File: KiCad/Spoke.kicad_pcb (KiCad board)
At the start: 2 copper layers, 50 x 100 mm, 128 parts, among them J1 B2B-PH-K-S, J10 BL-A, J11 BL-C, J12 Amphenol 132289, J2 BAT+, J3 BAT-, J4 GCT USB4105/USB4110, J5 CHG+, J6 CHG-, J7 PLS-1x3, J8 PLS-1x6, J9 PLS-1x3, Q1 AO3407A, Q2 AO3400, Q3 AO3400, Q4 AO3400, SW1 PWR, SW2 OK/UP, SW3 ESC/DN, SW4 BOOT, U1 SP0503BAHTG, U2 TP4056, U3 CP2102N-A02-GQFN28, U4 LM3671MF-3.3, U5 74HC4052PW, U6 STM32F103C8T6, U7 LSM303DLHC, X1 8MHz

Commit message: Add C14
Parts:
- added C14: 47uF, Spoke:C_tantA, B.Cu at (97.8, 89.5)
- moved C20 0.75 mm to (97.0, 91.5)
- renumbered C14 to C15, C15 to C16, C16 to C17, C17 to C18, C18 to C19, C19 to C20, C20 to C21, C21 to C22, C22 to C23, C23 to C24, C24 to C25, C25 to C26, C26 to C27, C27 to C28, C28 to C29, C29 to C30, C30 to C31, C31 to C32, C32 to C33
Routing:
- net +3V3: track 313.7 -> 318.9 mm, vias 14 -> 15
- net LED_RED: track 50.3 -> 52.1 mm
- net USB_RXD: track 85.4 -> 84.8 mm
- net GND: vias 20 -> 21

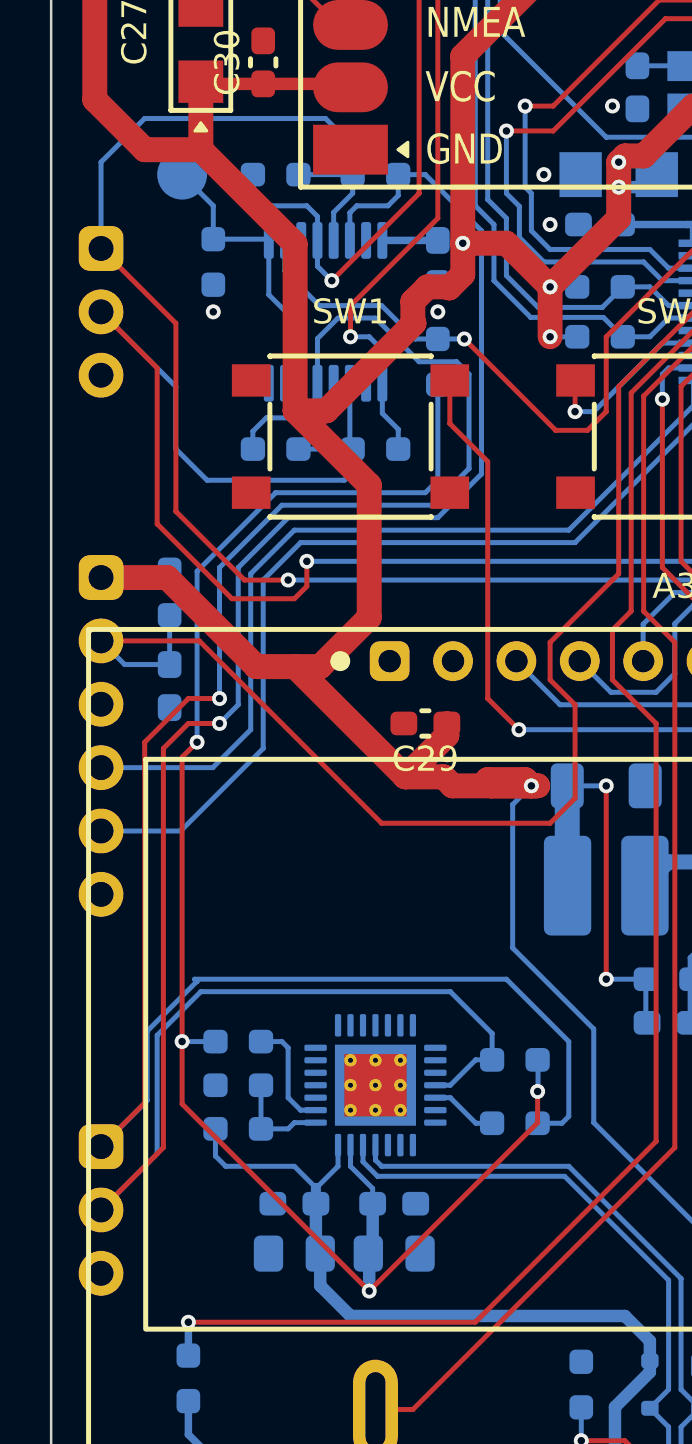
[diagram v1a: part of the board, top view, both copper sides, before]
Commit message: Add TP1, TP2
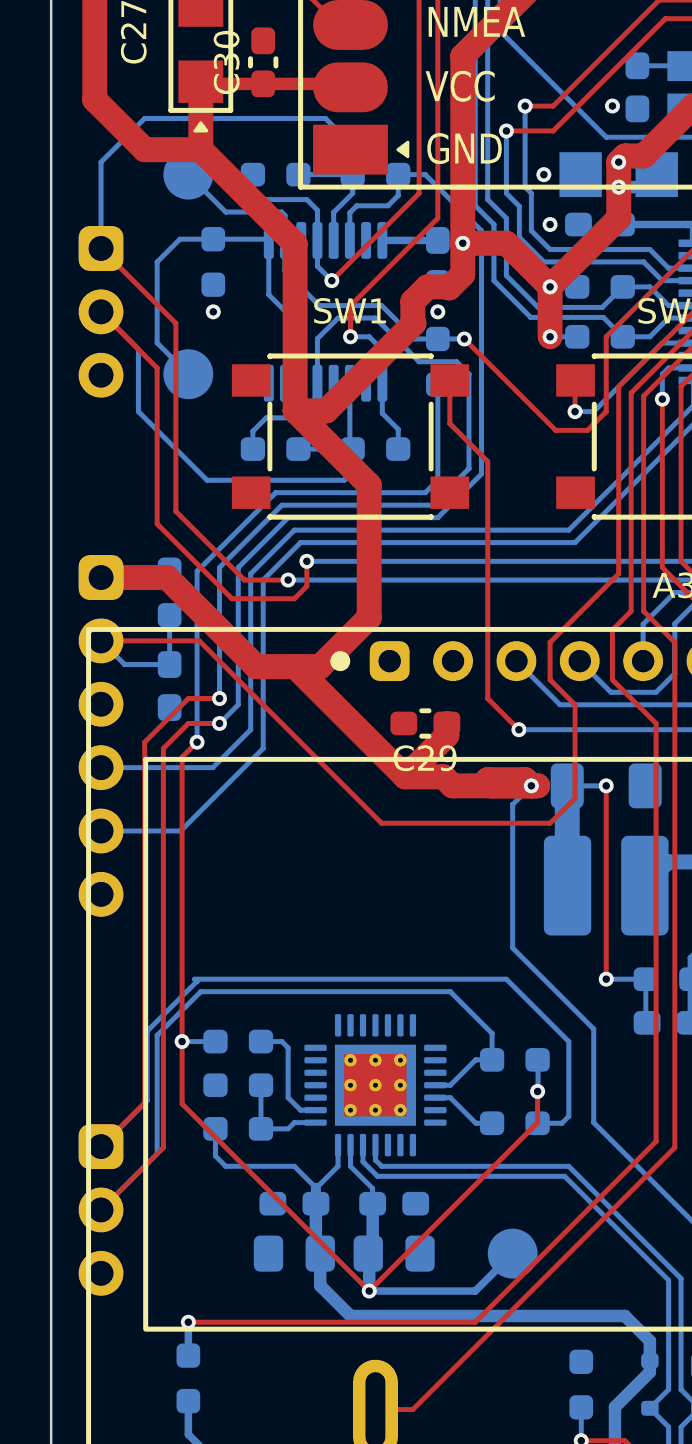
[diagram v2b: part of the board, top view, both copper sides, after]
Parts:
- added TP1: Pad-Round, Spoke:Pad_round, B.Cu at (93.5, 132.8)
- added TP2: Pad-Round, Spoke:Pad_round, B.Cu at (80.5, 89.5)
- moved TP3 8.00 mm to (80.5, 97.5)
- renumbered TP8 to TP10, TP9 to TP11, TP10 to TP12, TP11 to TP13, TP12 to TP14, TP13 to TP15, TP14 to TP16, TP15 to TP17, TP16 to TP18, TP1 to TP3, TP2 to TP4, TP3 to TP5, TP4 to TP6, TP5 to TP7, TP6 to TP8, TP7 to TP9
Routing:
- net VDD: track 66.9 -> 73.3 mm
- net MUX_BLE_USB: track 28.7 -> 34.2 mm
- net Net-(U5-S1): track 11.6 -> 16.2 mm

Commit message: Route BLE
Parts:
- moved TP10 2.75 mm to (79.0, 58.5)
- moved TP11 2.75 mm to (81.8, 58.5)
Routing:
- net +3V3: track 318.9 -> 334.4 mm
- net Net-(A1-SWDCLK): track 0.00 -> 14.4 mm, vias 0 -> 2
- net Net-(A1-SWDIO): track 0.00 -> 13.8 mm, vias 0 -> 2
- net Net-(A1-MODE): track 0.00 -> 8.52 mm
- net Net-(A1-DISC): track 0.00 -> 8.37 mm
- net Net-(A1-WAKEUP/SLEEP): track 0.00 -> 8.08 mm
- net Net-(A1-TXD): track 0.00 -> 5.57 mm
- net Net-(A1-nRESET): track 0.00 -> 5.08 mm
- net BLE_RXD: track 33.2 -> 38.2 mm
- net Net-(A1-LINK): track 0.00 -> 3.67 mm
- net Net-(A1-DATA): track 0.00 -> 3.34 mm
- net BLE_TXD: track 27.2 -> 29.8 mm

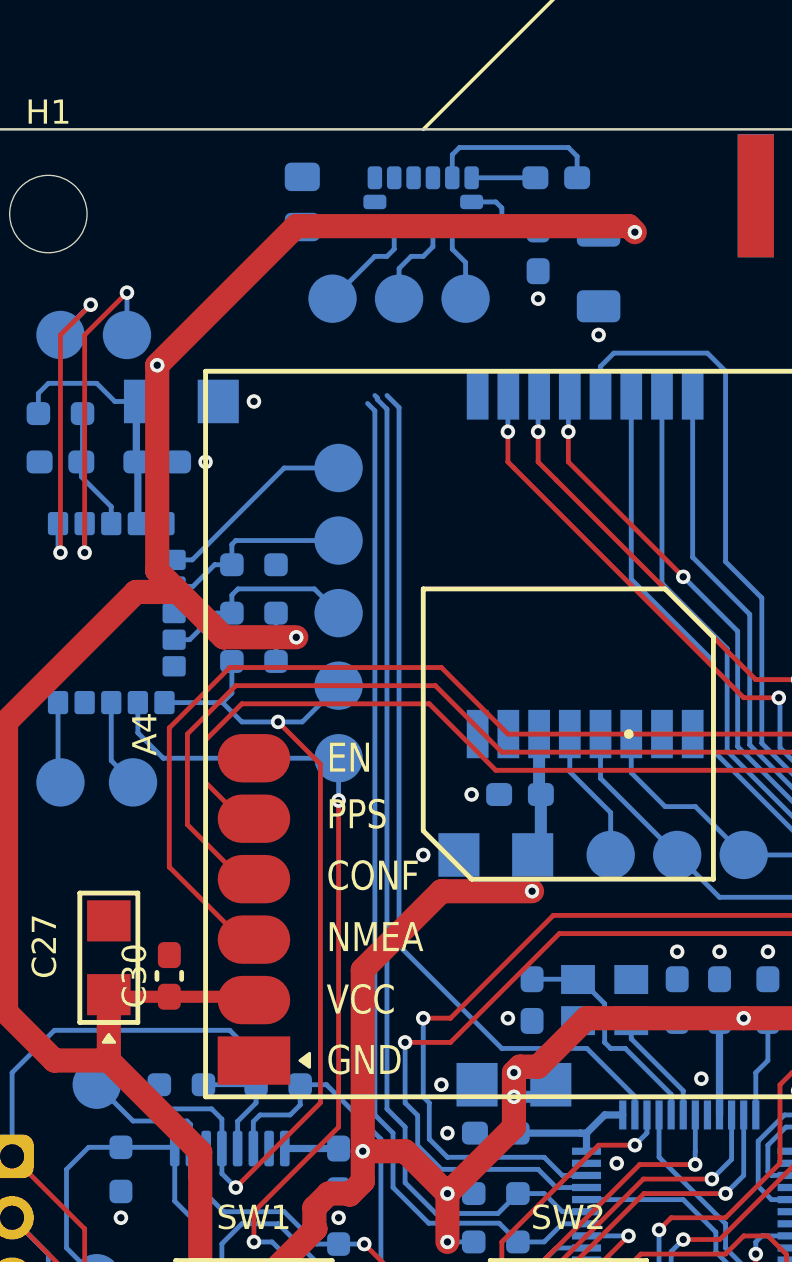
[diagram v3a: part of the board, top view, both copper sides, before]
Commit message: Route Compass
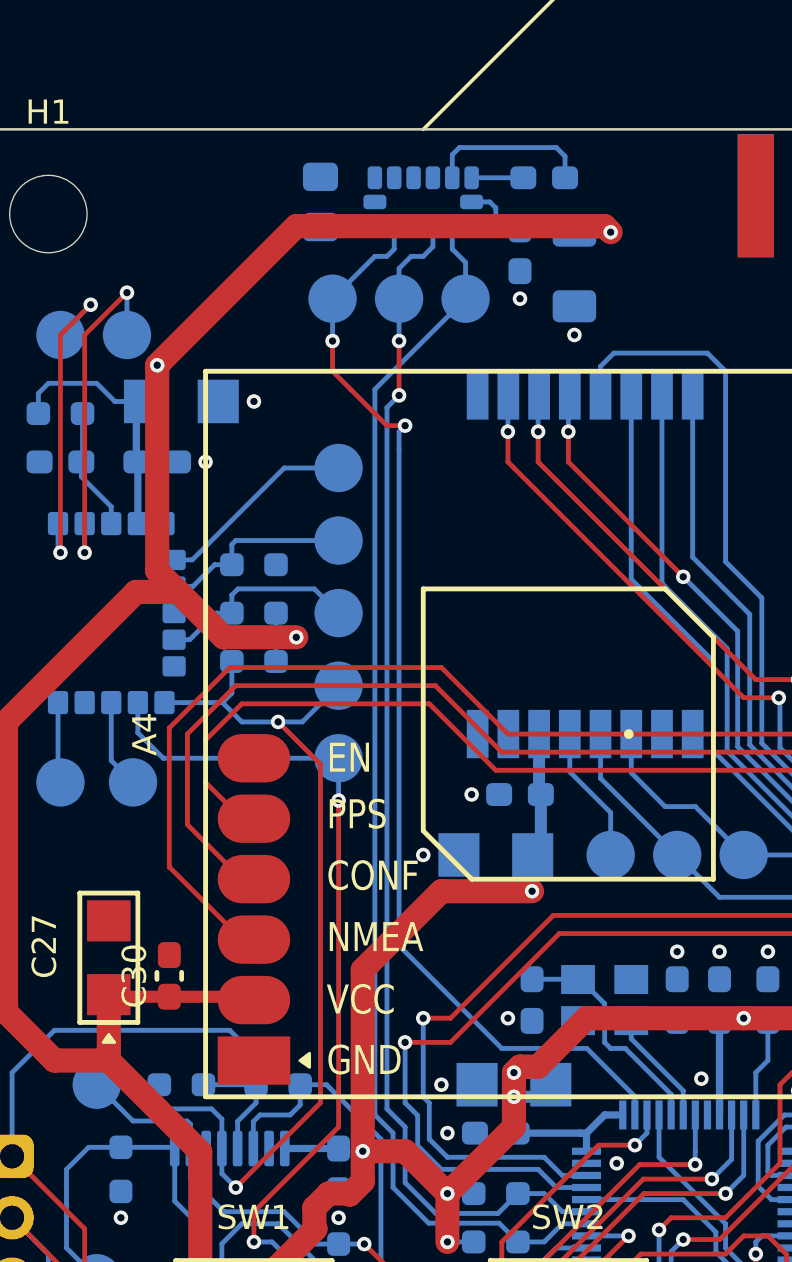
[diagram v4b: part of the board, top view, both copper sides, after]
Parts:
- moved C31 1.00 mm to (100.2, 55.8)
- moved C28 0.75 mm to (89.8, 53.0)
- moved C32 0.75 mm to (98.0, 55.0)
- moved C33 0.50 mm to (99.0, 52.0)
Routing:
- net I2C_SCL: track 45.3 -> 51.1 mm
- net I2C_INT: track 40.4 -> 46.0 mm, vias 0 -> 2
- net I2C_SDA: track 45.6 -> 49.6 mm, vias 0 -> 2
- net +3V3: track 334.4 -> 336.2 mm
- net Net-(U7-C1): track 3.02 -> 2.27 mm
- net Net-(U7-SETP): track 7.27 -> 6.77 mm
- net Net-(U7-SETC): track 2.64 -> 2.14 mm

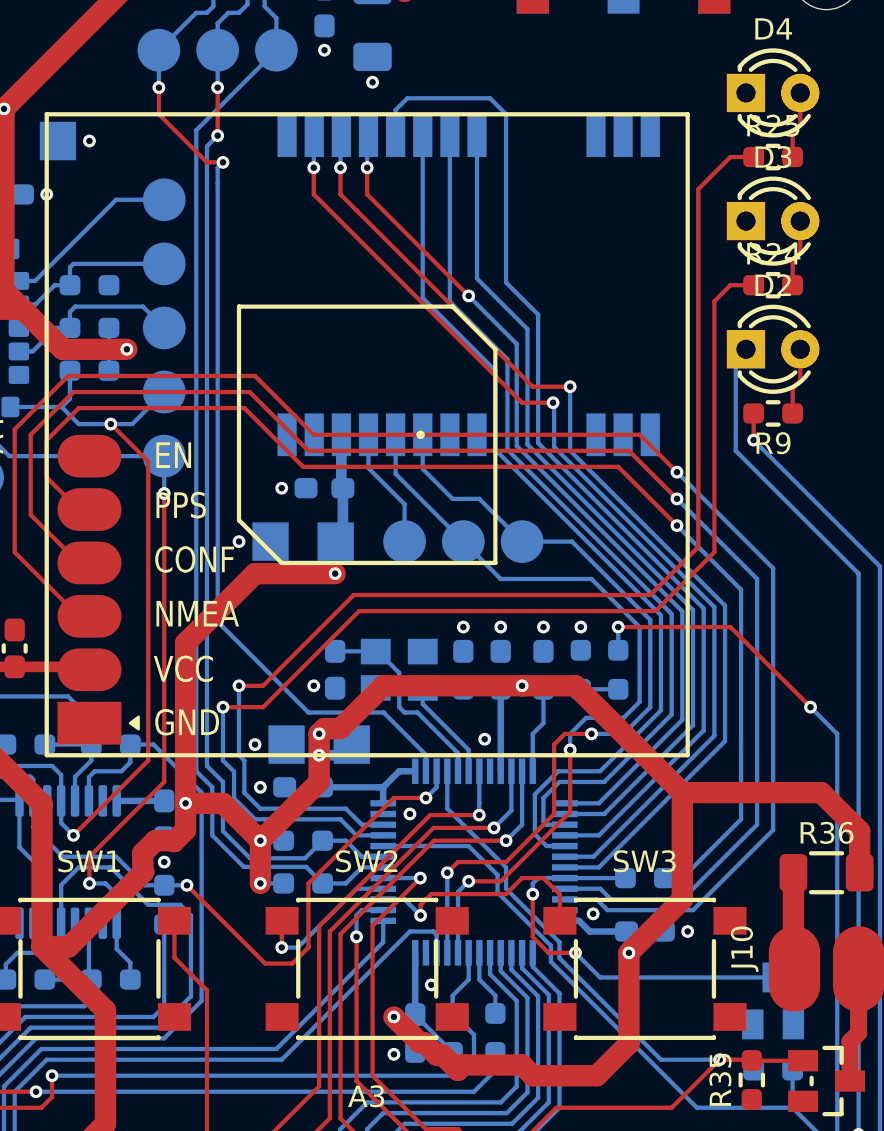
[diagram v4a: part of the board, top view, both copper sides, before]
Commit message: Modify C14 routing
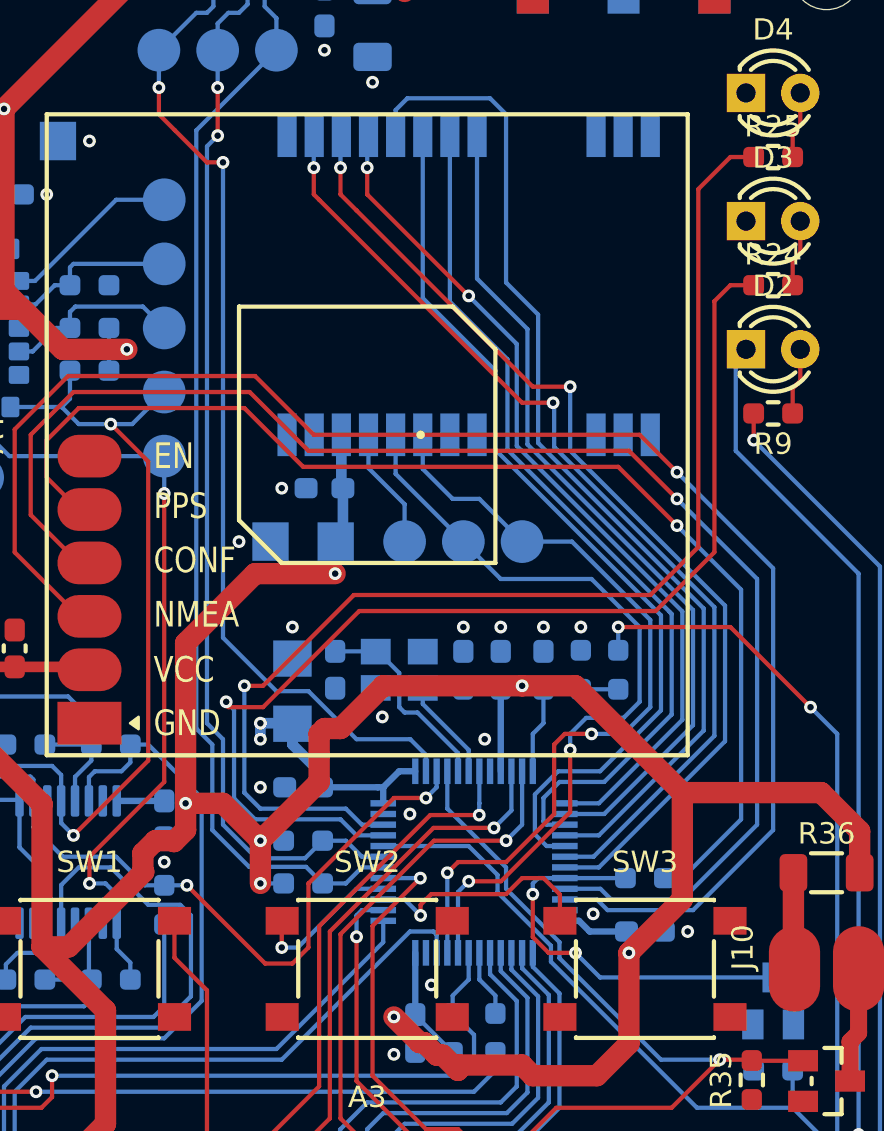
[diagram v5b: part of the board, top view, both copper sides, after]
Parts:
- moved C14 2.80 mm to (96.5, 87.0), turned to 90 degrees
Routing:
- net +3V3: track 336.2 -> 337.1 mm

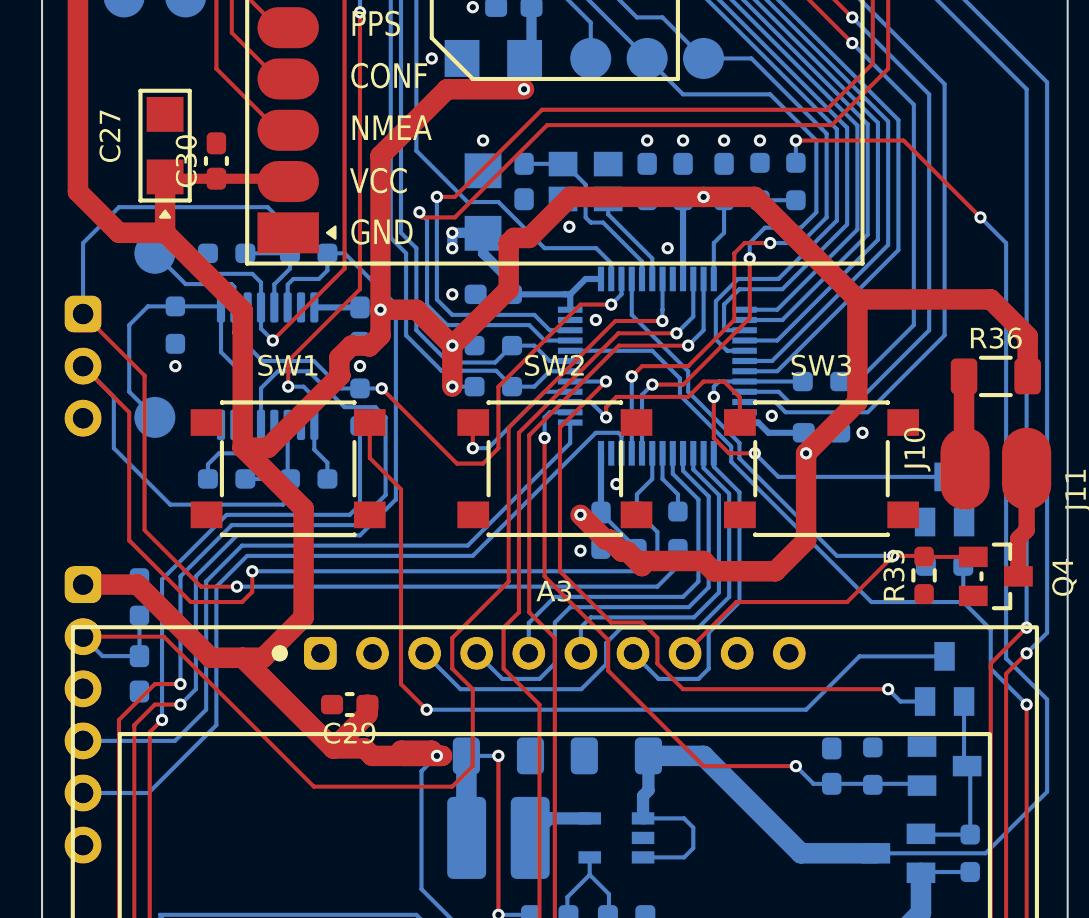
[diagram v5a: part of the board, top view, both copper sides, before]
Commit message: Routing mainly done; VCC left
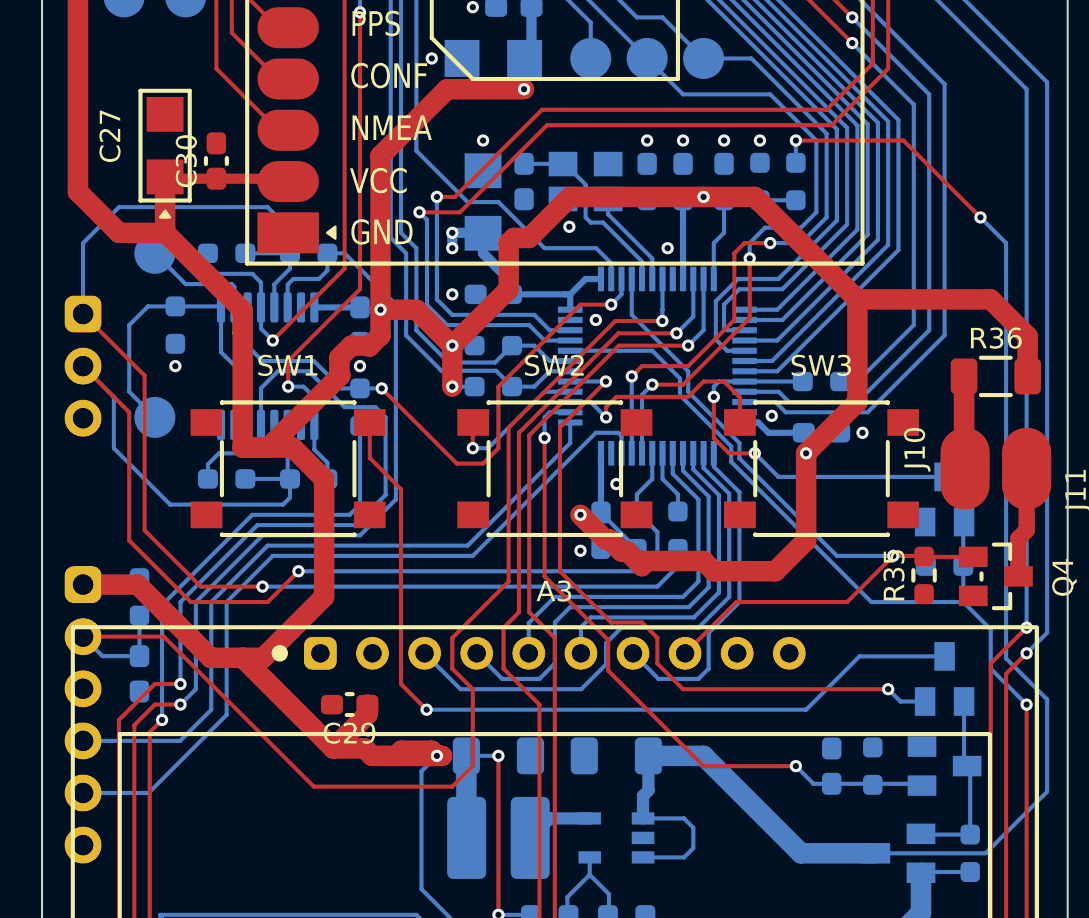
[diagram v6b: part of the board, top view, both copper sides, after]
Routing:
- net +3V3: track 337.1 -> 339.4 mm
- net BOOT0: track 62.2 -> 64.4 mm
- net USB_TXD: track 84.1 -> 83.4 mm
- net USB_RXD: track 84.6 -> 83.9 mm
- net SWD_IO: track 38.4 -> 37.7 mm
- net VDD: track 73.3 -> 72.6 mm
- net SWD_CLK: track 34.4 -> 33.8 mm
- net CONSOLE_RXD: track 64.1 -> 63.5 mm
